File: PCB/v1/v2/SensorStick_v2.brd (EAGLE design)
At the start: 50.8 x 50.8 mm, 62 parts, among them IC1 STM32L412RBT6, J1 DST310S_32.768KHZ, J2 10118192-0001LF, U1 BMI088, U2 LD39050PU33R, Y1 8MHz

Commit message: Jesus - More merge changes
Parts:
- removed C2, C37: 4.7p, GQM2195C2E4R7BB12D(4_7p):CAPC2012X100N
- removed C3, C35: 20p, CC0402KPX7R7BB104(0402cap_foot):CAPC1005X55N
- removed J1: DST310S_32.768KHZ, ce-capstone-2022:DST310S_32.768KHZ_DST310S32768KHZ
- removed R4: 220, RC0805FR-10220RL:RESC2012X60N
- removed Y1: 8MHz, ce-capstone:XTAL_ABLS-8.000MHZ-B2-T
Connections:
- removed net N$3: C3.1, R4.2, Y1.1
- removed net PC14-OSC32-IN: C37.1, J1.1
- removed net PC15-OSC32-OUT: C2.1, J1.2
- removed net PH0-OSC-IN: C35.1, Y1.2
- removed net PH1-OSC-OUT: R4.1
- net GND: no longer C2.2, C3.2, C35.2, C37.2
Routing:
- net TIM2_CH4: track 33.4 -> 0.00 mm, vias 2 -> 0
- net TIM2_CH3: track 28.3 -> 0.00 mm, vias 2 -> 0
- net TIM2_CH1: track 26.7 -> 0.00 mm, vias 2 -> 0
- net TIM15_CH1: track 24.0 -> 0.00 mm, vias 2 -> 0
- net TIM16_CH1: track 23.7 -> 0.00 mm, vias 2 -> 0
- net PH0-OSC-IN: track 23.5 -> 0.00 mm
- net TIM2_CH2: track 22.6 -> 0.00 mm, vias 2 -> 0
- net I2C2_SDA: track 26.0 -> 5.40 mm, vias 2 -> 1
- net I2C2_SCL: track 21.3 -> 3.94 mm, vias 2 -> 1
- net PH1-OSC-OUT: track 16.6 -> 0.00 mm
- net PC14-OSC32-IN: track 13.8 -> 0.00 mm
- net GND: track 113.6 -> 104.1 mm, vias 55 -> 52
- net TIM15_CH2: track 21.5 -> 13.7 mm, vias 2 -> 1
- net N$3: track 7.65 -> 0.00 mm
- net PC15-OSC32-OUT: track 5.56 -> 0.00 mm
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
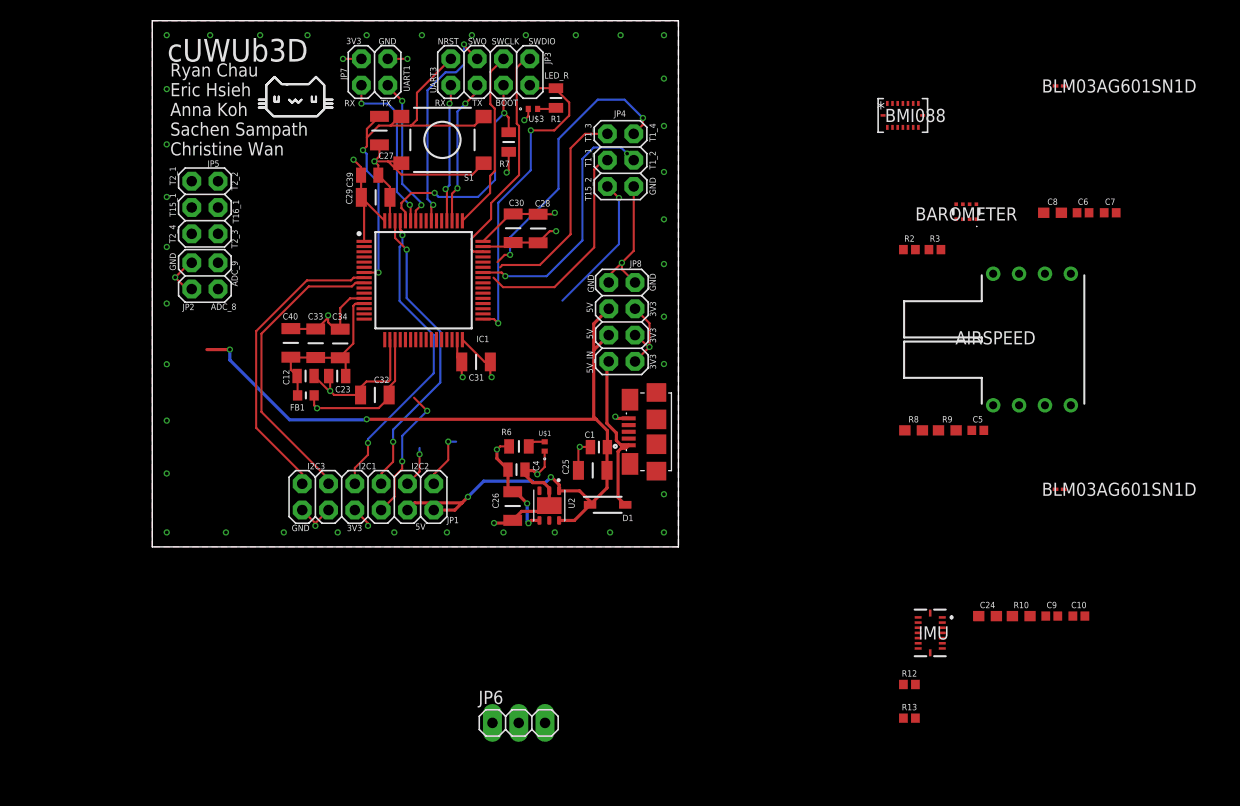
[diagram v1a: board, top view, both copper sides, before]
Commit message: Jesus - Schematic should be complete
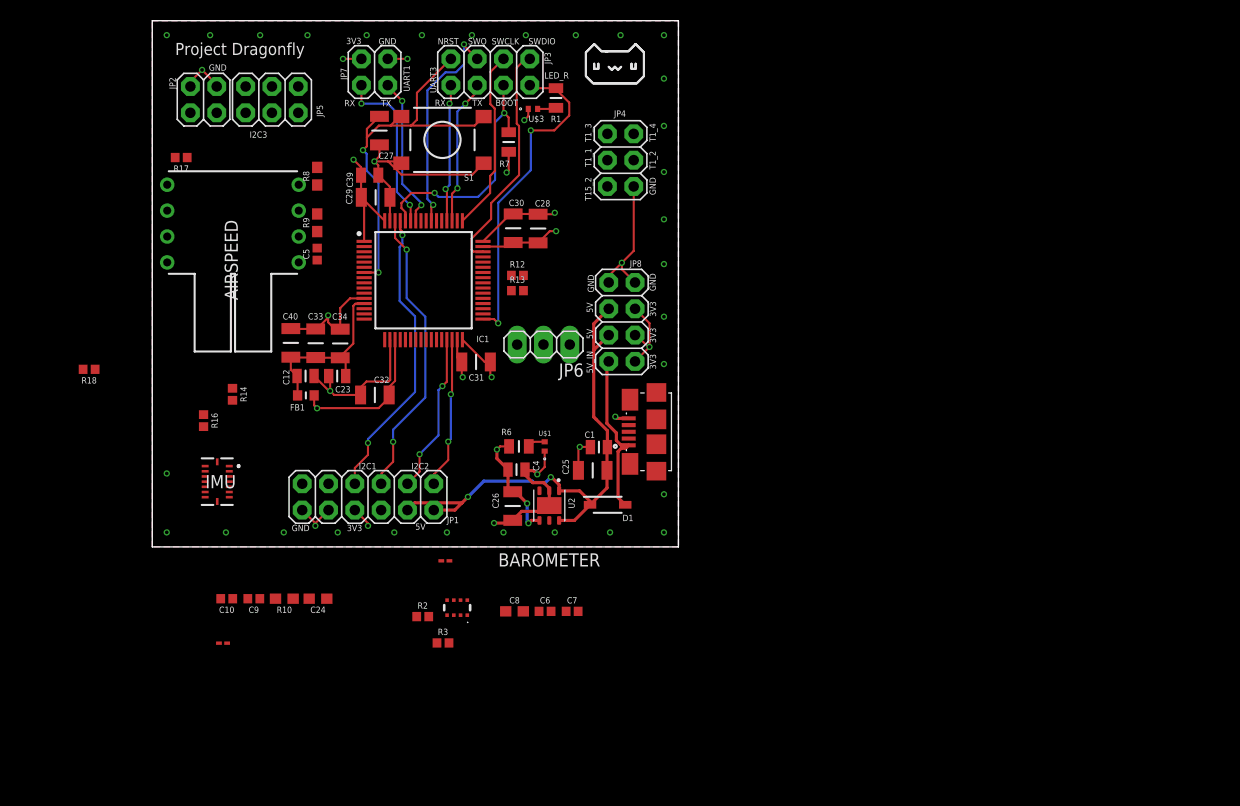
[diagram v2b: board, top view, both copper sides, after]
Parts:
- removed U1: BMI088, BMI088:QFN_BMI085_BOS
- added R14, R16, R17, R18: 22, SparkFun-Resistors:0402
- moved C10 82.3 mm to (7.19, -5.00), turned to 180 degrees
- moved L3 82.1 mm to (6.83, -9.30)
- moved C9 77.1 mm to (9.80, -5.00), turned to 180 degrees
- moved L7 75.0 mm to (28.3, -1.35)
- moved AIRSPEED 74.4 mm to (5.84, 26.4), turned to 90 degrees
- moved R10 71.2 mm to (12.8, -5.00), turned to 180 degrees
- moved IMU 70.4 mm to (6.27, 6.30)
- moved C5 66.0 mm to (15.9, 28.3), turned to 90 degrees
- moved C24 64.7 mm to (16.0, -5.00), turned to 180 degrees
- moved C6 64.6 mm to (37.9, -6.22)
- moved C8 64.6 mm to (35.0, -6.22)
- moved C7 64.6 mm to (40.5, -6.22)
- moved R9 64.0 mm to (15.9, 31.3), turned to 90 degrees
- moved R8 62.6 mm to (15.9, 35.8), turned to 90 degrees
- moved BAROMETER 62.3 mm to (29.4, -5.87)
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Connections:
- net TIM16_CH1 renamed I2C3_SCL1
- net TIM2_CH3 renamed I2C3_SDA1
- removed net ADC1_IN9: JP2.2
- removed net ADC2_IN8: JP2.4
- removed net PC5: JP1.7
- removed net SPIO_EXTI2: IC1.28
- removed net TIM15_CH1: JP5.3
- removed net TIM15_CH2: JP4.5
- removed net TIM1_CH1: JP4.3
- removed net TIM1_CH2: JP4.4
- removed net TIM1_CH3: JP4.1
- removed net TIM1_CH4: JP4.2
- removed net TIM2_CH1: JP5.1
- removed net TIM2_CH2: JP5.2
- removed net TIM2_CH4: JP5.5
- removed net VDD: U1.3
- removed net VDDIO: U1.11
- new net EXTI4: R18.2
- new net GPIO_EXTI2: IC1.28, R16.1
- net EXTI0: now also R14.2
- net EXTI2: now also R16.2
- net EXTI3: now also R17.2
- net GPIO_EXTI0: now also R14.1
- net GPIO_EXTI3: now also R17.1
- net GPIO_EXTI4: now also R18.1
- net I2C3_SCL: no longer JP1.2
- net I2C3_SDA: no longer JP1.4
- net SPI1_MISO: now also JP1.4
- net SPI1_MOSI: now also JP1.7
- net SPI1_SCK: now also JP1.2
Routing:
- net 5V: track 91.2 -> 50.1 mm, vias 4 -> 2
- net I2C3_SCL: track 29.1 -> 0.00 mm
- net I2C3_SDA: track 29.1 -> 0.01 mm
- net TIM1_CH4: track 27.0 -> 0.00 mm, vias 2 -> 0
- net TIM1_CH2: track 25.0 -> 0.00 mm, vias 2 -> 0
- net TIM1_CH1: track 20.9 -> 0.00 mm
- net TIM1_CH3: track 20.6 -> 0.00 mm
- net TIM15_CH2: track 13.7 -> 0.00 mm, vias 1 -> 0
- net PC5: track 13.2 -> 0.00 mm, vias 2 -> 0
- net I2C2_SCL: track 3.94 -> 15.5 mm, vias 1 -> 2
- net I2C2_SDA: track 5.40 -> 14.6 mm, vias 1 -> 2
- net I2C1_SCL: track 30.1 -> 28.6 mm
- net I2C1_SDA: track 29.6 -> 28.4 mm
- net GND: vias 52 -> 45
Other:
- board text added: "Project Dragonfly"
- board text removed: "ADC_8"
- board text removed: "ADC_9"
- board text removed: "Ryan Chau Eric Hsieh Anna Koh Sachen Sampath Christine Wan"
- board text removed: "T15_1"
- board text removed: "T16_1"
- board text removed: "T2_1"
- board text removed: "T2_2"
- board text removed: "T2_3"
- board text removed: "T2_4"
- board text removed: "cUWUb3D"

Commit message: Jesus - Updates to header pins on sch
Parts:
- moved R18 30.7 mm to (24.1, 22.5)
- moved JP2 24.3 mm to (4.83, 18.9), turned to 270 degrees
- moved C24 18.2 mm to (3.56, 8.33)
- moved BAROMETER 15.9 mm to (31.9, -21.6)
- moved L3 12.8 mm to (5.69, 3.40)
- moved R17 12.6 mm to (15.4, 37.0), turned to 90 degrees
- moved C9 12.5 mm to (3.45, 5.79)
- moved C5 11.0 mm to (5.79, 24.0), turned to 0 degrees
- moved R10 8.99 mm to (11.2, 3.86), turned to 270 degrees
- moved R9 8.86 mm to (11.0, 24.0), turned to 0 degrees
- moved C10 8.48 mm to (8.46, 3.38)
- moved R8 8.39 mm to (15.5, 27.4)
- moved AIRSPEED 7.98 mm to (4.14, 34.2), turned to 0 degrees
- moved IMU 4.51 mm to (9.73, 9.19), turned to 180 degrees
- moved L7 3.86 mm to (25.6, -4.14)
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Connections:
- removed net I2C3_SCL1: JP5.4
- removed net I2C3_SDA1: JP5.6
- net I2C1_SCL: now also JP5.1; no longer JP1.6
- net I2C1_SDA: now also JP5.2; no longer JP1.8
- net I2C3_SCL: now also JP5.4
- net I2C3_SDA: now also JP2.2
- net SPI1_MOSI: now also JP1.6; no longer JP1.7
- net SPI1_SCK: now also JP2.4; no longer JP1.2
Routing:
- net I2C1_SCL: track 28.6 -> 0.00 mm, vias 2 -> 0
- net I2C1_SDA: track 28.4 -> 0.00 mm, vias 2 -> 0
- net I2C2_SCL: track 15.5 -> 0.00 mm, vias 2 -> 0
- net GPIO_EXTI3: track 0.00 -> 15.0 mm, vias 0 -> 2
- net I2C2_SDA: track 14.6 -> 0.00 mm, vias 2 -> 0
- net I2C3_SDA: track 0.01 -> 12.6 mm
- net SPI2_MOSI: track 0.00 -> 11.3 mm
- net I2C3_SCL: track 0.00 -> 9.74 mm
- net SPI2_MISO: track 0.00 -> 8.60 mm
- net 3V3: track 62.2 -> 69.1 mm, vias 10 -> 12
- net SPI2_SCK: track 0.00 -> 5.55 mm
- net EXTI3: track 0.00 -> 4.65 mm
- net GND: track 104.1 -> 107.6 mm, vias 45 -> 37
- net N$4: track 0.00 -> 3.04 mm
- net N$1: track 0.00 -> 2.85 mm

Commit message: Jesus - Updates to header pins on sch
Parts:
- removed BAROMETER: DPS310XTSA1, DPS310XTSA1:DPS310XTSA1
- added BAR: DPS310XTSA1, DPS310XTSA1:DPS310XTSA1
- moved R2 25.6 mm to (30.9, 15.0)
- moved R3 24.0 mm to (26.8, 11.9), turned to 270 degrees
- moved C7 22.0 mm to (33.1, 12.4), turned to 270 degrees
- moved C6 18.4 mm to (30.7, 8.76)
- moved C8 16.3 mm to (31.0, 7.24)
- moved L7 15.4 mm to (31.8, 9.98), turned to 180 degrees
- moved R18 14.1 mm to (24.3, 8.38), turned to 270 degrees
- moved R16 11.3 mm to (9.40, 1.78), turned to 180 degrees
- moved R10 10.3 mm to (2.11, 8.71), turned to 90 degrees
- moved L3 9.60 mm to (6.38, 13.0), turned to 180 degrees
- moved C9 9.34 mm to (8.10, 13.9), turned to 0 degrees
- moved C24 8.57 mm to (8.38, 15.4), turned to 0 degrees
- moved R14 3.51 mm to (4.32, 14.0)
- moved JP6 3.09 mm to (38.3, 16.5)
- moved C10 2.39 mm to (10.8, 3.35), turned to 0 degrees
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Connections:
- net 3V3: now also BAR.2, BAR.5, BAR.6; no longer BAROMETER.2, BAROMETER.5, BAROMETER.6
- net EXTI2: now also JP1.2
- net EXTI4: now also JP1.8
- net GND: now also BAR.1, BAR.7; no longer BAROMETER.1, BAROMETER.7
- net I2C2_SCL: now also BAR.4, JP1.12; no longer BAROMETER.4, JP1.10
- net I2C2_SDA: now also BAR.3, JP1.10; no longer BAROMETER.3, JP1.12
- net N$6: now also BAR.8; no longer BAROMETER.8
- net USB_DN: now also JP4.5
- net USB_DP: now also JP4.3
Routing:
- net CSB_ACCEL: track 0.00 -> 61.9 mm, vias 0 -> 2
- net CSB_GYRO: track 0.00 -> 43.1 mm, vias 0 -> 2
- net SPI1_MISO: track 0.00 -> 40.1 mm, vias 0 -> 2
- net SPI1_SCK: track 0.00 -> 37.8 mm
- net SPI1_MOSI: track 0.00 -> 33.0 mm, vias 0 -> 2
- net GPIO_EXTI2: track 0.00 -> 30.3 mm, vias 0 -> 2
- net 3V3: track 69.1 -> 97.1 mm, vias 12 -> 17
- net GPIO_EXTI0: track 0.00 -> 24.9 mm, vias 0 -> 2
- net I2C1_SCL: track 0.00 -> 22.5 mm, vias 0 -> 2
- net GND: track 107.6 -> 129.7 mm, vias 37 -> 23
- net I2C3_SCL: track 9.74 -> 30.3 mm
- net I2C2_SDA: track 0.00 -> 20.6 mm, vias 0 -> 2
- net I2C2_SCL: track 0.00 -> 20.0 mm, vias 0 -> 2
- net I2C1_SDA: track 0.00 -> 20.0 mm, vias 0 -> 2
- net USB_DP: track 0.00 -> 19.5 mm
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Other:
- board text added: "Danny C Teagan C Noah L Jesus O Marko R"
- board text added: "SPI1"
- board text added: "SPI2"
- board text added: "Thanks to HandLED Team"
- board text removed: "T15_2"
- board text removed: "T1_1"
- board text removed: "T1_2"
- board text removed: "T1_3"
- board text removed: "T1_4"

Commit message: J & N - Added TCXO to sch
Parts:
- added R11: 22, SparkFun-Resistors:0402
- added Y1: ECS-TXO-3225MV-400-TR, SamacSys_Parts:ECSTXO3225MV400TR
- moved R17 24.6 mm to (-9.14, 35.4), turned to 180 degrees
- moved AIRSPEED 14.8 mm to (-6.99, 24.5), turned to 90 degrees
- moved R8 12.3 mm to (5.13, 33.9)
- moved R9 9.71 mm to (3.63, 30.3), turned to 270 degrees
- moved C5 3.96 mm to (3.61, 27.3), turned to 90 degrees
- moved R10 2.55 mm to (-0.43, 8.97)
- moved JP2 2.08 mm to (3.17, 20.2)
- moved C24 1.53 mm to (9.02, 16.8)
- moved R14 0.65 mm to (4.95, 14.1)
- moved L3 0.65 mm to (7.01, 13.1)
- moved C10 0.65 mm to (11.5, 3.48)
- moved R16 0.65 mm to (10.0, 1.91)
- moved C9 0.65 mm to (8.74, 14.0)
- moved IMU 0.65 mm to (8.69, 8.94)
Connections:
- new net N$3: R11.1, Y1.3
- net 3V3: now also Y1.1, Y1.4
- net GND: now also Y1.2
- net OSC_IN: now also R11.2
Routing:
- net GPIO_EXTI3: track 15.0 -> 38.1 mm
- net 3V3: track 97.1 -> 116.3 mm, vias 17 -> 20
- net CSB_ACCEL: track 61.9 -> 52.4 mm
- net I2C3_SDA: track 20.5 -> 29.4 mm
- net I2C3_SCL: track 30.3 -> 36.4 mm
- net GND: track 129.7 -> 134.9 mm, vias 23 -> 24
- net IMU_INT4: track 12.0 -> 16.6 mm
- net OSC_IN: track 0.00 -> 3.77 mm
- net N$3: track 0.00 -> 3.67 mm
- net EXTI0: track 6.89 -> 10.1 mm
- net NRST: track 40.1 -> 43.4 mm, vias 0 -> 2
- net SPI1_SCK: track 37.8 -> 40.5 mm
- net IMU_INT2: track 6.20 -> 8.87 mm
- net GPIO_EXTI2: track 30.3 -> 32.7 mm
- net EXTI2: track 17.5 -> 15.8 mm
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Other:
- board size 50.8 x 50.8 mm -> 63.5 x 50.8 mm
